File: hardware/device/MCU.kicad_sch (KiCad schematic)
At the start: 20 parts, among them J4 EXPANSION, SW24 NRST, U18 STM32H743ZIT6

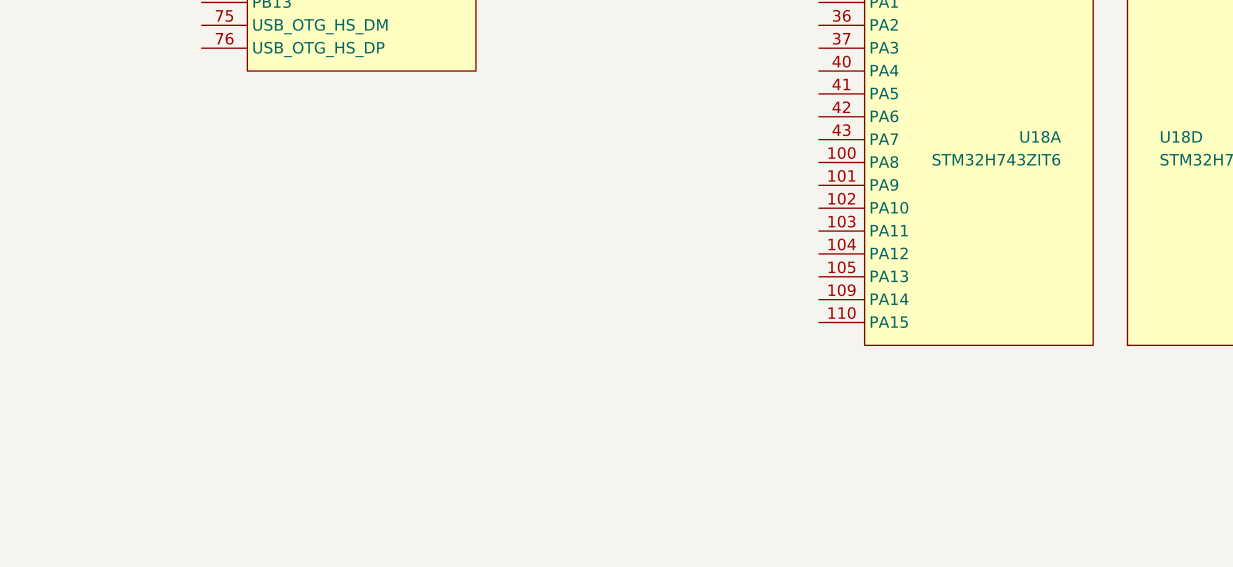
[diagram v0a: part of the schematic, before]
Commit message: feat: start codec layout
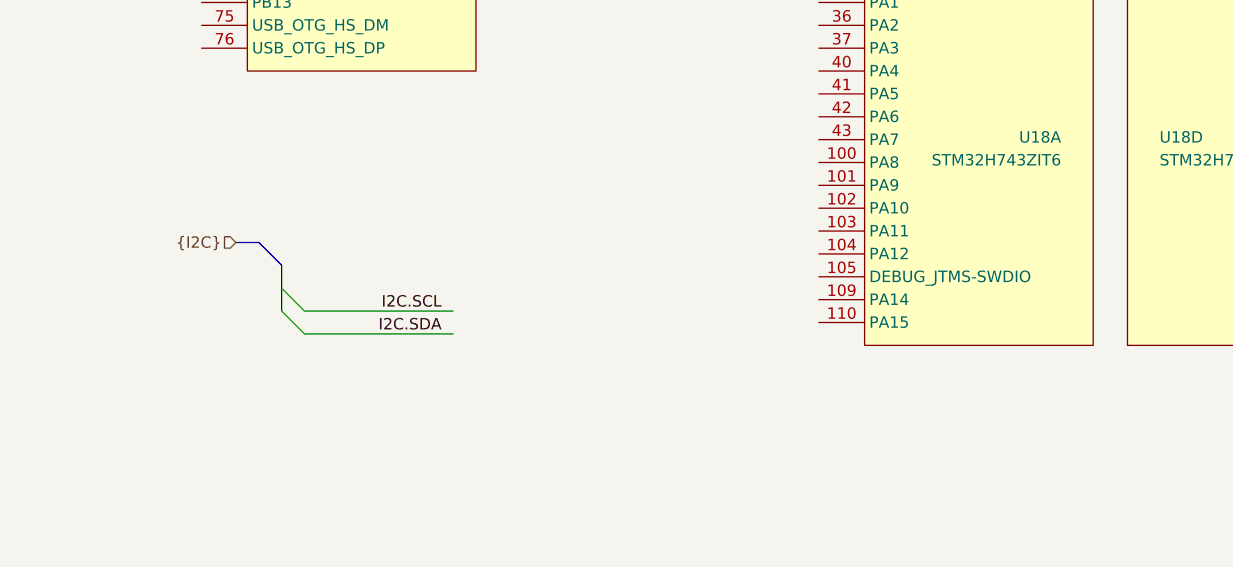
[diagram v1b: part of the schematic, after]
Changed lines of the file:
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@@
 	)
 	(bus_entry
+		(at 142.24 160.02)
+		(size -2.54 -2.54)
+		(stroke
+			(width 0)
+			(type default)
+		)
+	)
+	(bus_entry
 		(at 276.86 109.22)
 		(size 2.54 -2.54)
@@
 	)
 	(bus_entry
+		(at 142.24 157.48)
+		(size -2.54 -2.54)
+		(stroke
+			(width 0)
+			(type default)
+		)
+	)
+	(bus_entry
 		(at 276.86 76.2)
 		(size 2.54 -2.54)
@@
 		)
 	)
+	(bus
+		(pts
+			(xy 139.7 154.94) (xy 139.7 157.48)
+		)
+		(stroke
+			(width 0)
+			(type default)
+		)
+	)
 	(wire
 		(pts
@@
 	(bus
 		(pts
+			(xy 134.62 149.86) (xy 137.16 149.86)
+		)
+		(stroke
+			(width 0)
+			(type default)
+		)
+	)
+	(bus
+		(pts
 			(xy 184.15 71.12) (xy 184.15 76.2)
 		)
@@
 		)
 	)
+	(bus
+		(pts
+			(xy 139.7 152.4) (xy 139.7 154.94)
+		)
+		(stroke
+			(width 0)
+			(type default)
+		)
+	)
 	(wire
 		(pts
@@
 		)
 	)
+	(wire
+		(pts
+			(xy 142.24 160.02) (xy 158.75 160.02)
+		)
+		(stroke
+			(width 0)
+			(type default)
+		)
+	)
 	(bus
 		(pts
@@
 		)
 	)
+	(bus
+		(pts
+			(xy 139.7 152.4) (xy 137.16 149.86)
+		)
+		(stroke
+			(width 0)
+			(type default)
+		)
+	)
 	(wire
 		(pts
@@
 		)
 	)
+	(wire
+		(pts
+			(xy 142.24 157.48) (xy 158.75 157.48)
+		)
+		(stroke
+			(width 0)
+			(type default)
+		)
+	)
 	(bus
 		(pts
@@
 		)
 	)
+	(label "I2C.SDA"
+		(at 157.48 160.02 180)
+		(effects
+			(font
+				(size 1.27 1.27)
+			)
+			(justify right bottom)
+		)
+	)
 	(label "FMC.D10"
 		(at 265.43 59.69 0)
@@
 		)
 	)
+	(label "I2C.SCL"
+		(at 157.48 157.48 180)
+		(effects
+			(font
+				(size 1.27 1.27)
+			)
+			(justify right bottom)
+		)
+	)
 	(label "FMC.CAS"
 		(at 198.12 64.77 180)
@@
 		)
 	)
+	(hierarchical_label "{I2C}"
+		(shape input)
+		(at 134.62 149.86 180)
+		(effects
+			(font
+				(size 1.27 1.27)
+			)
+			(justify right)
+		)
+	)
 	(hierarchical_label "{FMC}"
 		(shape output)
@@
 		)
 		(pin "105"
+			(alternate "DEBUG_JTMS-SWDIO")
 		)
 		(pin "109"

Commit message: feat: various layouts, changed SDRAM to BGA
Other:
- moved on the sheet: U18A, U18C, U18D, U18E, U18F, U18G

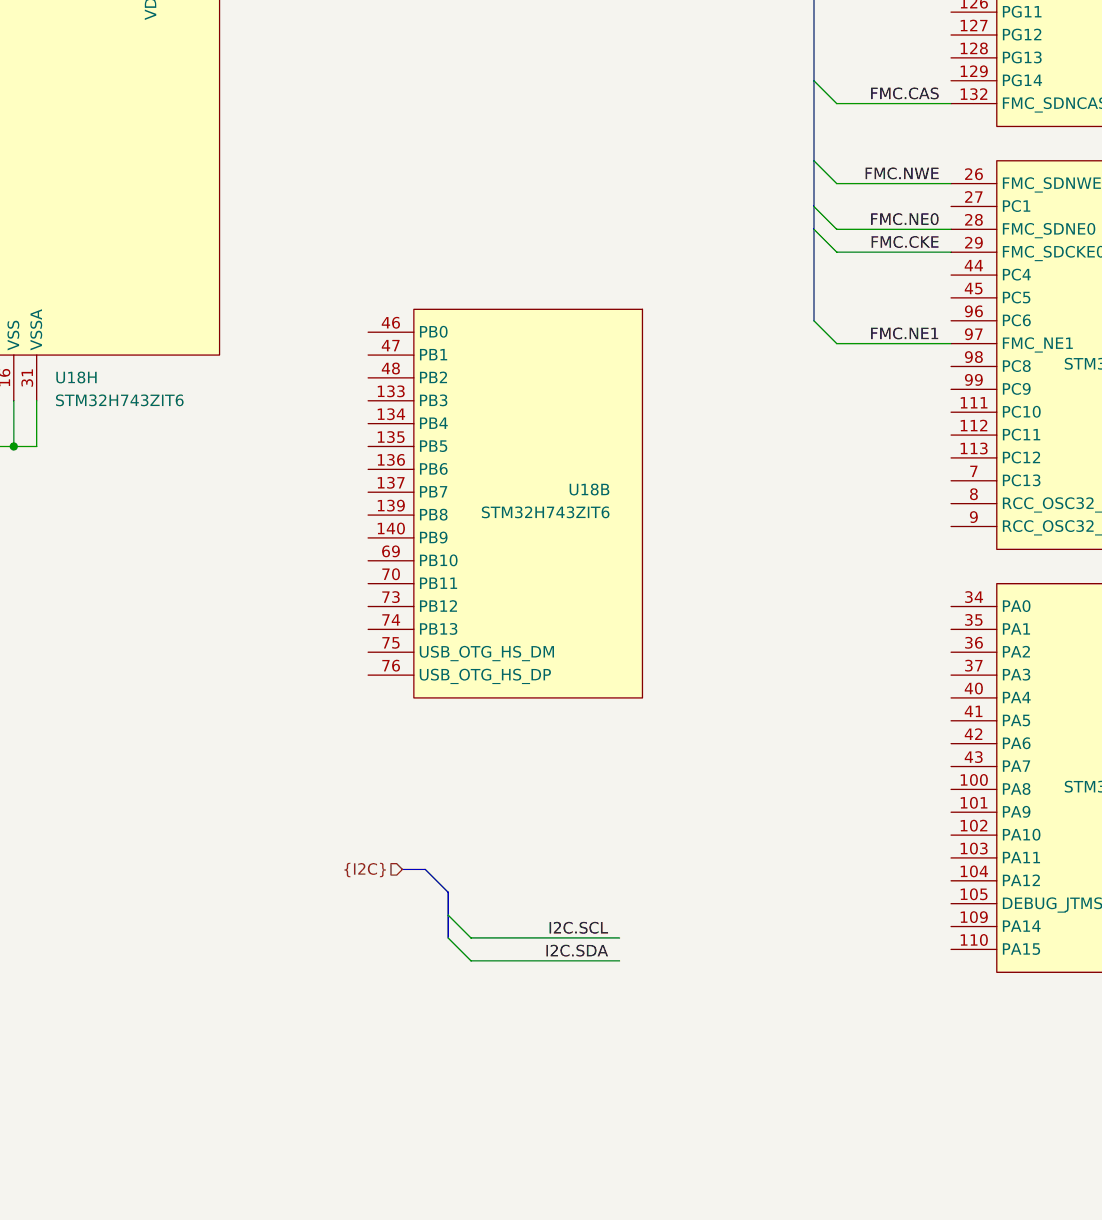
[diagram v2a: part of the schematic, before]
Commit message: feat: BGA routing for SDRAM
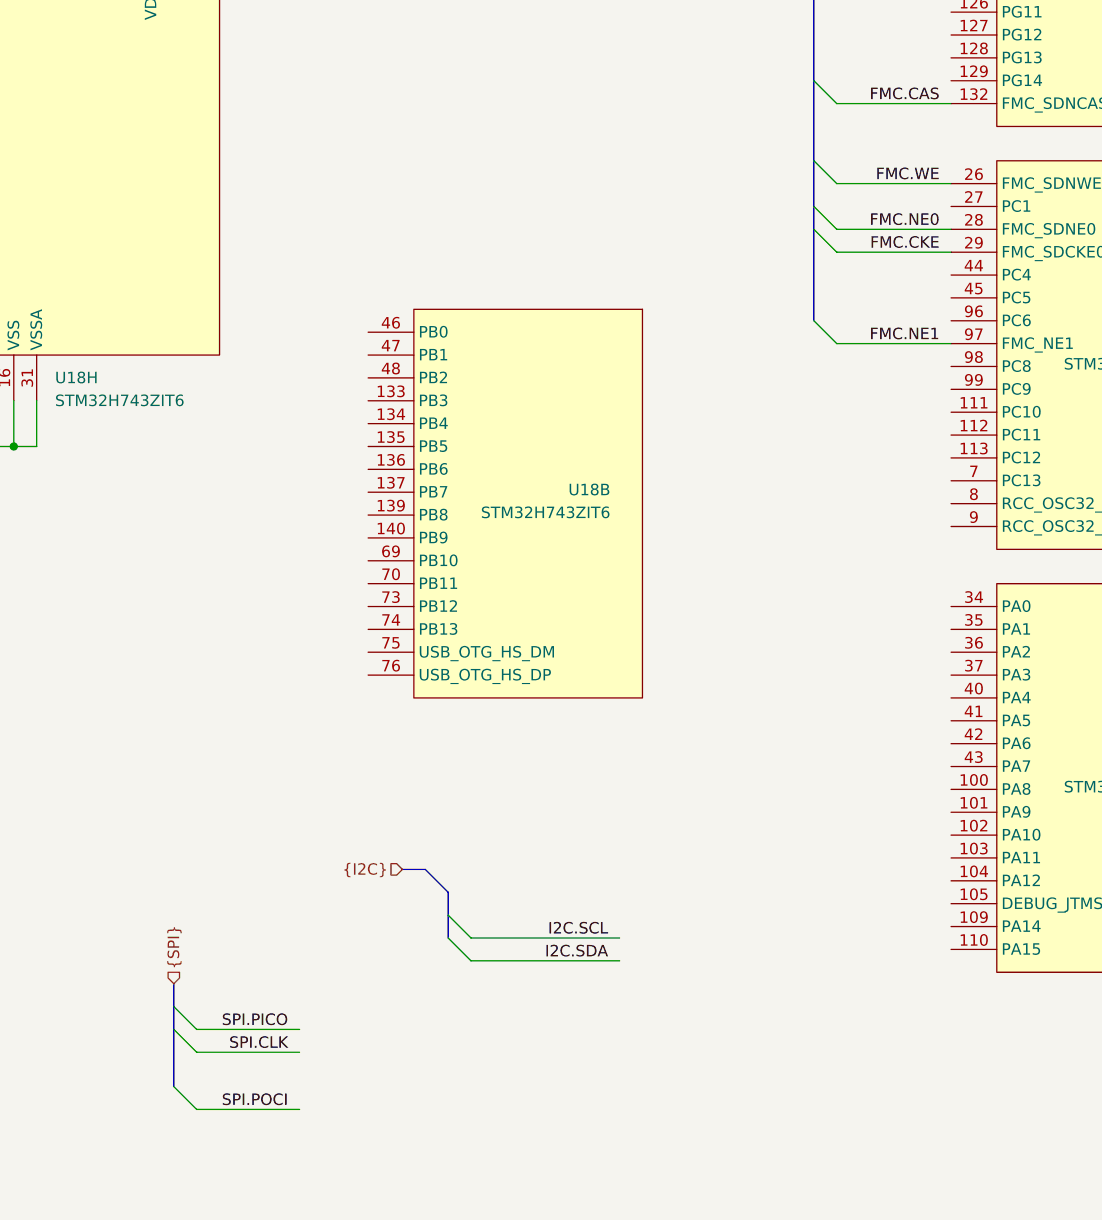
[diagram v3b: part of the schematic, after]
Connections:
- net FMC.NWE: no longer U18.26 (PC0)
- new net FMC.WE: U18.26 (PC0)
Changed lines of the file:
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@@
 	(generator_version "9.0")
 	(paper "A4")
+	(bus_alias "I2C"
+		(members "I2C.SCL" "I2C.SDA")
+	)
+	(bus_alias "SPI"
+		(members "SPI.PICO" "SPI.CLK" "SPI.POCI")
+	)
 	(text "1x 100nf per VDD"
 		(exclude_from_sim no)
@@
 	)
 	(bus_entry
+		(at 111.76 170.18)
+		(size -2.54 -2.54)
+		(stroke
+			(width 0)
+			(type default)
+		)
+	)
+	(bus_entry
 		(at 142.24 160.02)
 		(size -2.54 -2.54)
@@
 	)
 	(bus_entry
+		(at 111.76 167.64)
+		(size -2.54 -2.54)
+		(stroke
+			(width 0)
+			(type default)
+		)
+	)
+	(bus_entry
 		(at 273.05 143.51)
 		(size 2.54 -2.54)
@@
 	)
 	(bus_entry
+		(at 111.76 176.53)
+		(size -2.54 -2.54)
+		(stroke
+			(width 0)
+			(type default)
+		)
+	)
+	(bus_entry
 		(at 182.88 64.77)
 		(size -2.54 -2.54)
@@
 	(wire
 		(pts
+			(xy 111.76 176.53) (xy 123.19 176.53)
+		)
+		(stroke
+			(width 0)
+			(type default)
+		)
+	)
+	(wire
+		(pts
 			(xy 30.48 62.23) (xy 24.13 62.23)
 		)
@@
 	(bus
 		(pts
+			(xy 109.22 162.56) (xy 109.22 165.1)
+		)
+		(stroke
+			(width 0)
+			(type default)
+		)
+	)
+	(bus
+		(pts
 			(xy 273.05 17.78) (xy 275.59 20.32)
 		)
@@
 	(wire
 		(pts
+			(xy 111.76 170.18) (xy 123.19 170.18)
+		)
+		(stroke
+			(width 0)
+			(type default)
+		)
+	)
+	(wire
+		(pts
 			(xy 30.48 162.56) (xy 33.02 162.56)
 		)
@@
 		)
 	)
+	(bus
+		(pts
+			(xy 109.22 165.1) (xy 109.22 167.64)
+		)
+		(stroke
+			(width 0)
+			(type default)
+		)
+	)
 	(wire
 		(pts
@@
 		)
 	)
+	(bus
+		(pts
+			(xy 109.22 167.64) (xy 109.22 173.99)
+		)
+		(stroke
+			(width 0)
+			(type default)
+		)
+	)
 	(wire
 		(pts
@@
 		(pts
 			(xy 182.88 78.74) (xy 195.58 78.74)
+		)
+		(stroke
+			(width 0)
+			(type default)
+		)
+	)
+	(wire
+		(pts
+			(xy 111.76 167.64) (xy 123.19 167.64)
 		)
 		(stroke
@@
 		)
 	)
-	(label "FMC.NWE"
+	(label "FMC.WE"
 		(at 194.31 73.66 180)
 		(effects
@@
 		)
 	)
+	(label "SPI.POCI"
+		(at 121.92 176.53 180)
+		(effects
+			(font
+				(size 1.27 1.27)
+			)
+			(justify right bottom)
+		)
+	)
 	(label "FMC.D13"
 		(at 261.62 140.97 0)
@@
 		)
 	)
+	(label "SPI.CLK"
+		(at 121.92 170.18 180)
+		(effects
+			(font
+				(size 1.27 1.27)
+			)
+			(justify right bottom)
+		)
+	)
 	(label "FMC.BA1"
 		(at 194.31 39.37 180)
@@
 			)
 			(justify left bottom)
+		)
+	)
+	(label "SPI.PICO"
+		(at 121.92 167.64 180)
+		(effects
+			(font
+				(size 1.27 1.27)
+			)
+			(justify right bottom)
 		)
 	)
@@
 		)
 	)
+	(hierarchical_label "{SPI}"
+		(shape input)
+		(at 109.22 162.56 90)
+		(effects
+			(font
+				(size 1.27 1.27)
+			)
+			(justify left)
+		)
+	)

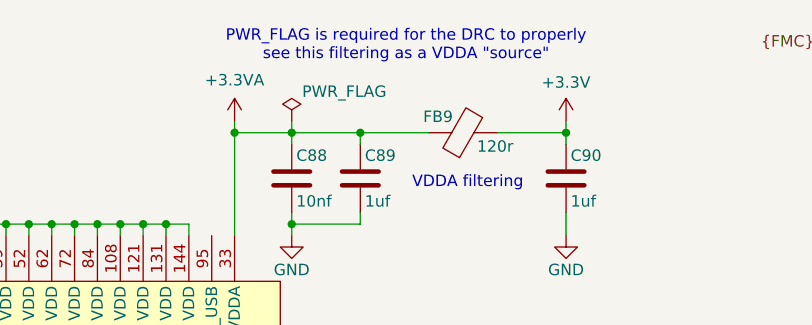
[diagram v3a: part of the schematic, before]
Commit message: feat: display FPC routing
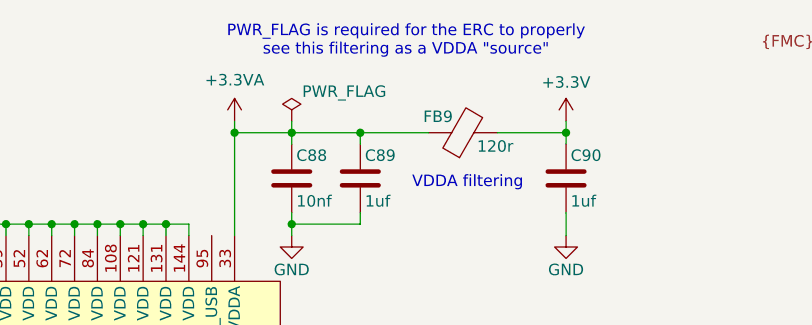
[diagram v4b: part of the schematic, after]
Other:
- note added: "PWR_FLAG is required for the ERC to properly see this filtering as a VDDA "source""
- note removed: "PWR_FLAG is required for the DRC to properly see this filtering as a VDDA "source""
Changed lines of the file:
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@@
 		)
 	)
-	(text "PWR_FLAG is required for the DRC to properly\nsee this filtering as a VDDA \"source\""
+	(text "PWR_FLAG is required for the ERC to properly\nsee this filtering as a VDDA \"source\""
 		(exclude_from_sim no)
-		(at 128.27 18.288 0)
+		(at 128.27 17.78 0)
 		(effects
 			(font

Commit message: feat: various audio and power schematic layout
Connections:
- net CODEC.MCLK: now reaches U18.1 (PE2)
- net CODEC.ADCDAT: now reaches U18.2 (PE3)
- net CODEC.LRCLK: now reaches U18.3 (PE4)
- net CODEC.BCLK: now reaches U18.4 (PE5)
- net CODEC.DACDAT: now reaches U18.5 (PE6)
- net USB_D-: now reaches U18.75 (PB14)
- net USB_D+: now reaches U18.76 (PB15)
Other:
- note added: "MCU signal to control soft power-off"
- note added: "Notifies MCU of line-in jack plug"
- note added: "Reads the state of the power switch for soft power-off"
- moved on the sheet: U18A, U18C, U18D, U18E, U18F, U18G
